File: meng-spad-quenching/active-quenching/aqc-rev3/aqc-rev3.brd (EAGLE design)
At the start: 120 x 74.9 mm, 274 parts, among them IC1 TPS7A4901, IC10 TPS7A3001, IC11 LT1534-1, IC12 74AHC1G04DCK, IC13 TLV271DBV, IC14 NC7WZ16P6X, IC15 LTC1711, IC16 HFA3134, IC17 HFA3135, IC18 USBLC6-2SC6Y, IC19 HFA3135, IC2 TPS7A4901, IC20 HFA3134, IC21 STM32F411RE, IC22 MAX572X, IC23 HFA3134, IC24 LM1117, IC25 HFA3134, IC26 THAT320, IC27 74AHC1G14DCK, IC28 NL17SZ125, IC29 TLV272DGK, IC3 LT1534-1, IC30 74AHC1G32DCK, IC31 74AHC1G08DCK, IC4 TLV272DGK, IC5 ADCMP582, IC6 DS1100LU-20+, IC7 HFA3134, IC8 NC7SV74K8X, IC9 HFA3134, M2 BSS806N, M3 BSS806N, Q6 IRLML6402TRPBF, SW1 MCU_RST, T1 MMBTH10, U1 MCP4725, U2 SN65EPT22DGK, U3 SN65EPT21DGK, X1 CONN_PULLDN_SENSE, X2 CONN_FORCE_QUENCH, X3 KEYSTONE-7774, X4 CONN_SPAD, X5 CONN_PHOTON_COUNTER, X6 KEYSTONE-7774, X7 CONN_SMU, X8 PN61729-S

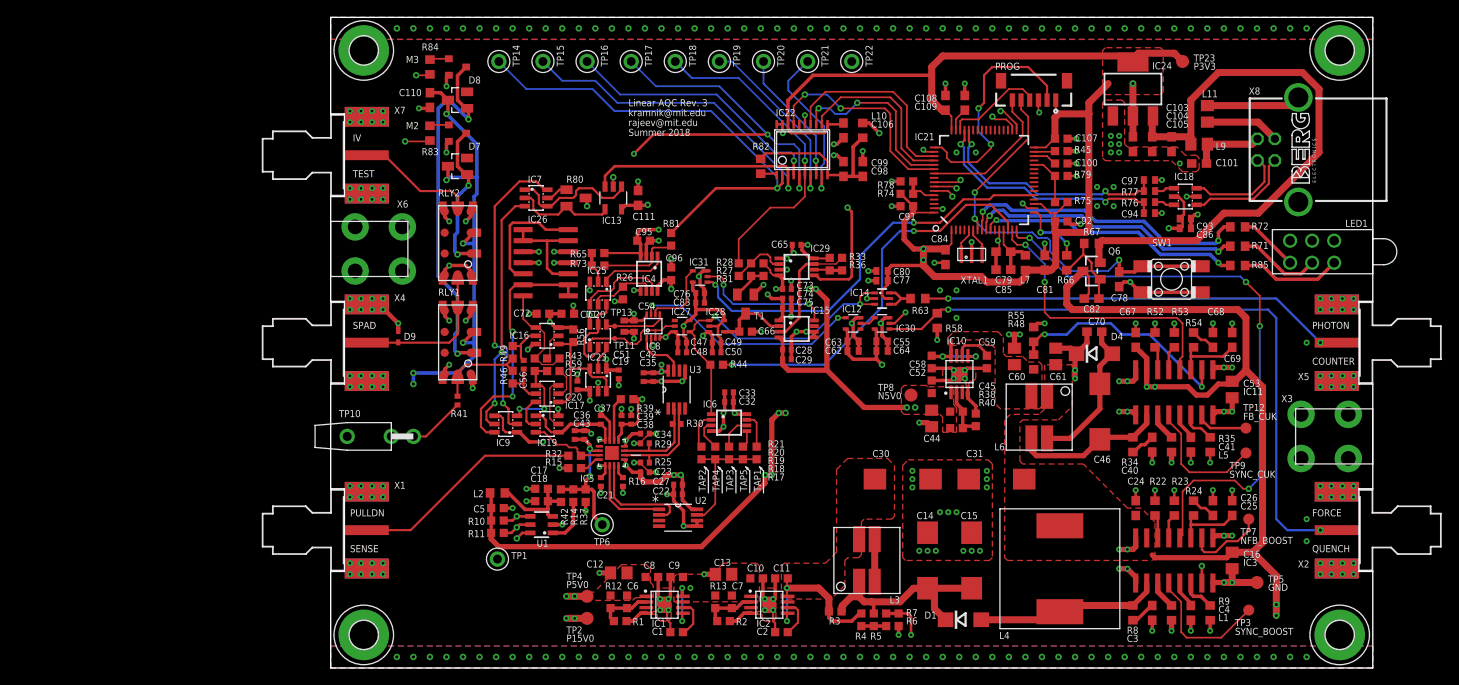
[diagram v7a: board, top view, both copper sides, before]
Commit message: Fixed one-shot error, layout done
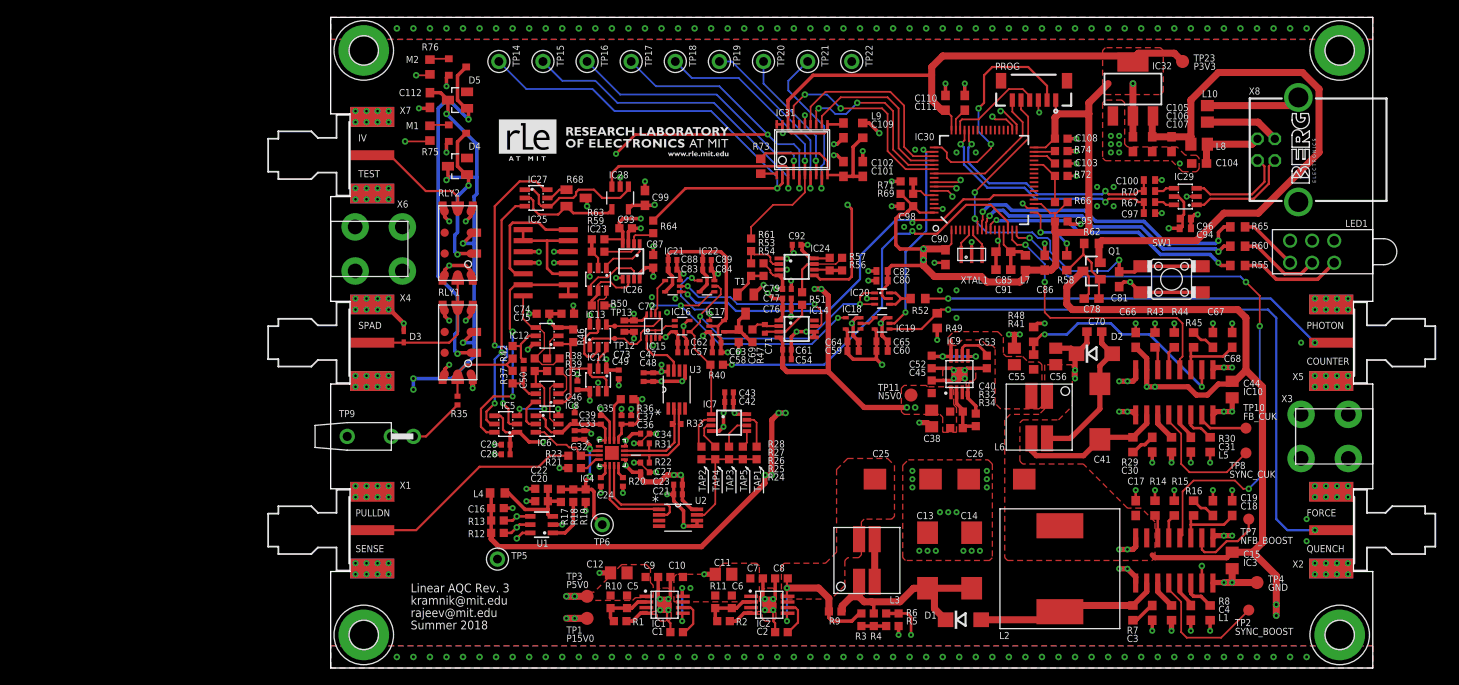
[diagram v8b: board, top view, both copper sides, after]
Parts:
- removed D7: BAS40, diode:SOT23
- removed D9: (no value), diode:SOD523
- removed L11: MI0805J102R-10, meng:R0805
- removed M3: BSS806N, meng:SOT23R_INFINEON
- removed R78: 0R, rcl-modified-footprints:R0603
- removed R79: DNP, rcl-modified-footprints:R0603
- removed R81: 220k, rcl-modified-footprints:R0603
- removed R82: 0R, rcl:R0603
- removed R83, R84: 100R, rcl:R0603
- removed R85: 470R, resistor:R0603
- added C102: 4u7, rcl:C0603
- added C112, C90: 100n, rcl:C0603
- added C87: 100n, rcl-modified-footprints:C0603
- added C88, C89: 100n, rcl-modified-footprints:C0402
- added D2: CDBA140SL-HF, diode:DO214AC
- added D3: TVS, diode:SOD523
- added DNP1000: RLE_LOGO, meng:RLE_LOGO
- added IC32: LM1117, meng:SOT-223
- added L8: MI0805J102R-10, meng:R0805
- added M1: BSS806N, meng:SOT23R_INFINEON
- added R47, R51: 0R, rcl-modified-footprints:R0603
- added R50: 110R, 1%, rcl-modified-footprints:R0603
- added R57: 100k, rcl-modified-footprints:R0603
- added R60: 470R, resistor:R0603
- added R61: 220k, rcl-modified-footprints:R0603
- added R62: 100k, resistor:R0603
- added R64: 102k, 1%, rcl-modified-footprints:R0603
- added R69: DNP, rcl-modified-footprints:R0603
- C100: value 100n -> 47p; device rcl-modified-footprints:C0603 -> rcl:C0402
- C101, C23, C28, C36, C42, C45, C7, C76, C78: value 10n -> 100n
- C103, C108, C40, C98: device rcl:C0603 -> rcl-modified-footprints:C0603
- C104, C21, C27, C29, C43, C5, C80, C83: value 100n -> 10n
- C105, C99: value 4u7 -> 100n
- C107: value 100n -> 4u7; device rcl-modified-footprints:C0603 -> rcl:C0603
- C11: value 100n -> 10u; device rcl-modified-footprints:C0603 -> rcl:C0805
- C13: value 10u -> 47u, 20V; device rcl:C0805 -> rcl:CT7343
- C15: value 47u, 20V -> 4u7; device rcl:CT7343 -> rcl:C0805
- C16: value 4u7 -> 100n; device rcl:C0805 -> rcl-modified-footprints:C0603
- C17: value 4u7 -> 100n; device rcl-modified-footprints:C0603 -> rcl:C0603
- C18: value 100n -> 15n; device rcl-modified-footprints:C0603 -> rcl:C0603
- C19: value 10n -> 220p; device rcl-modified-footprints:C0402 -> rcl:C0603
- C20: value 10n -> 100n; device rcl-modified-footprints:C0402 -> rcl-modified-footprints:C0603
- C22: value 10n -> 4u7; device rcl-modified-footprints:C0402 -> rcl-modified-footprints:C0603
- C24, C84: value 100n -> 10n; device rcl:C0603 -> rcl-modified-footprints:C0402
- C25: value 15n -> 47u, 20V; device rcl:C0603 -> rcl:CT7343
- C26: value 220p -> 47u, 20V; device rcl:C0603 -> rcl:CT7343
- C30: value 47u, 20V -> 10n; device rcl:CT7343 -> rcl:C0603
- C31: value 47u, 20V -> 1300p; device rcl:CT7343 -> rcl:C0603
- C38: value 100n -> 10u; device rcl-modified-footprints:C0402 -> rcl:C0805
- C41: value 1300p -> 68u, 16V; device rcl:C0603 -> rcl:CT7343
- C44: value 10u -> 4u7
- C46: value 68u, 16V -> 10n; device rcl:CT7343 -> rcl-modified-footprints:C0402
- C50: value 100n -> 100p
- C51: device rcl:C0402 -> rcl-modified-footprints:C0603
- C53: value 4u7 -> 10n; device rcl:C0805 -> rcl-modified-footprints:C0603
- C54, C62, C77: device rcl:C0402 -> rcl-modified-footprints:C0402
- C55: value 10n -> 10u, 10V; device rcl:C0402 -> rcl:C0805
- C56: value 100p -> 4u7; device rcl-modified-footprints:C0402 -> rcl:C0805
- C57: value 10n -> 100n; device rcl-modified-footprints:C0603 -> rcl-modified-footprints:C0402
- C58, C92: device rcl-modified-footprints:C0603 -> rcl-modified-footprints:C0402
- C59: device rcl-modified-footprints:C0603 -> rcl:C0402
- C60: value 10u, 10V -> 100n; device rcl:C0805 -> rcl:C0402
- C61: value 4u7 -> 10n; device rcl:C0805 -> rcl-modified-footprints:C0402
- C63: value 100n -> 10n; device rcl:C0402 -> rcl-modified-footprints:C0402
- C65, C73: value 100n -> 10n; device rcl-modified-footprints:C0402 -> rcl:C0402
- C66: value 100p -> 100n; device rcl-modified-footprints:C0603 -> rcl:C0603
- C67: value 100n -> 33n
- C68: value 33n -> DNP
- C69: value DNP -> 100p; device rcl:C0603 -> rcl-modified-footprints:C0603
- C71: value 100n -> DNP; device rcl-modified-footprints:C0603 -> rcl-modified-footprints:C0402
- C72: value 10n -> 100n; device rcl-modified-footprints:C0603 -> rcl:C0402
- C74, C75: device rcl-modified-footprints:C0402 -> rcl-modified-footprints:C0603
- C79: value 4u7 -> 100n; device rcl:C0603 -> rcl-modified-footprints:C0402
- C81: value 4u7 -> 10n
- C82: device rcl:C0603 -> rcl:C0402
- C85: value 100n -> 4u7
- C86: value 100n -> 4u7; device rcl:C0402 -> rcl:C0603
- C91: device rcl-modified-footprints:C0603 -> rcl:C0603
- C93: value 10n -> 100n; device rcl:C0402 -> rcl-modified-footprints:C0603
- C94: value 47p -> 100n
- C96: value 100n -> 10n; device rcl-modified-footprints:C0603 -> rcl:C0402
- D4: value CDBA140SL-HF -> BAS40; device diode:DO214AC -> diode:SOT23
- IC10: value TPS7A3001 -> LT1534-1; device Kramnik's Library:MSOP-8_POWER_PAD -> meng:SO16
- IC11: value LT1534-1 -> HFA3134; device meng:SO16 -> meng:SOT23-6L
- IC12: value 74AHC1G04DCK -> HFA3134; device 74xx-little-de:SC70-5 -> meng:SOT23-6L
- IC13: value TLV271DBV -> HFA3134; device meng:SOT23-5 -> meng:SOT23-6L
- IC14: value NC7WZ16P6X -> LTC1711; device meng:SC70-6L -> meng:MSOP8
- IC15: value LTC1711 -> NC7SV74K8X; device meng:MSOP8 -> meng:US8_3.1MM_JDEC_MO-187
- IC16: value HFA3134 -> 74AHC1G14DCK; device meng:SOT23-6L -> 74xx-little-de:SC70-5
- IC17: value HFA3135 -> NL17SZ125; device meng:SOT23-6L -> 74xx-little-de:SC70-5
- IC18: value USBLC6-2SC6Y -> 74AHC1G04DCK; device meng:SOT23-6L -> 74xx-little-de:SC70-5
- IC19: value HFA3135 -> 74AHC1G32DCK; device meng:SOT23-6L -> 74xx-little-de:SC70-5
- IC20: value HFA3134 -> NC7WZ16P6X; device meng:SOT23-6L -> meng:SC70-6L
- IC21: value STM32F411RE -> 74AHC1G08DCK; device meng:TQFP64_STM32 -> 74xx-little-de:SC70-5
- IC22: value MAX572X -> 74AHC1G08DCK; device meng:TSSOP20 -> 74xx-little-de:SC70-5
- IC24: value LM1117 -> TLV272DGK; device meng:SOT-223 -> meng:MSOP8
- IC25: value HFA3134 -> THAT320; device meng:SOT23-6L -> meng:SO14
- IC26: value THAT320 -> TLV272DGK; device meng:SO14 -> meng:MSOP8
- IC27: value 74AHC1G14DCK -> HFA3134; device 74xx-little-de:SC70-5 -> meng:SOT23-6L
- IC28: value NL17SZ125 -> TLV271DBV; device 74xx-little-de:SC70-5 -> meng:SOT23-5
- IC29: value TLV272DGK -> USBLC6-2SC6Y; device meng:MSOP8 -> meng:SOT23-6L
- IC30: value 74AHC1G32DCK -> STM32F411RE; device 74xx-little-de:SC70-5 -> meng:TQFP64_STM32
- IC31: value 74AHC1G08DCK -> MAX572X; device 74xx-little-de:SC70-5 -> meng:TSSOP20
- IC4: value TLV272DGK -> ADCMP582; device meng:MSOP8 -> meng:QFN50P300X300X80-16N
- IC5: value ADCMP582 -> HFA3134; device meng:QFN50P300X300X80-16N -> meng:SOT23-6L
- IC6: value DS1100LU-20+ -> HFA3135; device meng:MSOP8 -> meng:SOT23-6L
- IC7: value HFA3134 -> DS1100LU-20+; device meng:SOT23-6L -> meng:MSOP8
- IC8: value NC7SV74K8X -> HFA3135; device meng:US8_3.1MM_JDEC_MO-187 -> meng:SOT23-6L
- IC9: value HFA3134 -> TPS7A3001; device meng:SOT23-6L -> Kramnik's Library:MSOP-8_POWER_PAD
- L10: value PE-0603FB601ST -> MI0805J102R-10; device meng:R0603 -> meng:R0805
- L2: value PE-0603FB601ST -> 732-1699-2-ND; device meng:R0603 -> meng:WE_INDUCTOR_SIZE_CODE_1210
- L4: value 732-1699-2-ND -> PE-0603FB601ST; device meng:WE_INDUCTOR_SIZE_CODE_1210 -> meng:R0603
- L9: value MI0805J102R-10 -> PE-0603FB601ST; device meng:R0805 -> meng:R0603
- R10: value 2k2 -> 76k8
- R11: value 2k2 -> 137k
- R12: value 76k8 -> 2k2
- R13: value 137k -> 2k2
- R14: device rcl-modified-footprints:R0603 -> resistor:R0603
- R15: value DNP -> 1k; device rcl-modified-footprints:R0603 -> resistor:R0603
- R16: value 49R9 -> 6k8; device rcl-modified-footprints:R0402 -> resistor:R0603
- R18: value DNP -> 1k
- R20: value DNP -> 49R9; device rcl-modified-footprints:R0603 -> rcl-modified-footprints:R0402
- R22: value 1k -> 150R; device resistor:R0603 -> rcl-modified-footprints:R0402
- R23: value 1k -> 220R, 1%; device resistor:R0603 -> rcl-modified-footprints:R0603
- R24: value 6k8 -> DNP; device resistor:R0603 -> rcl-modified-footprints:R0603
- R25: value 150R -> DNP; device rcl-modified-footprints:R0402 -> rcl-modified-footprints:R0603
- R26: value 220R -> DNP
- R27, R28: value 220k -> DNP
- R29: value 150R -> 100R; device rcl-modified-footprints:R0402 -> resistor:R0603
- R3, R74: value DNP -> 0R
- R30: value 100R -> 16k9; device rcl-modified-footprints:R0402 -> rcl:R0603
- R31: value 10k -> 150R; device rcl-modified-footprints:R0603 -> rcl-modified-footprints:R0402
- R32: value 220R -> 76k8
- R33: value 100k -> 100R; device rcl-modified-footprints:R0603 -> rcl-modified-footprints:R0402
- R34: value 100R -> 24k; device resistor:R0603 -> rcl-modified-footprints:R0603
- R35: value 16k9 -> 49R9; device rcl:R0603 -> rcl-modified-footprints:R0402
- R36: value 100k -> 10k
- R37, R42: value DNP -> 100R, 1%
- R38: value 76k8 -> 200R, 1%
- R39: value 10k -> 200R, 1%
- R4: value 0R -> DNP
- R40: value 24k -> 49R9
- R41: value 49R9 -> 1k4; device rcl-modified-footprints:R0402 -> resistor:R0603
- R43: value 220R -> 1k; device rcl-modified-footprints:R0603 -> resistor:R0603
- R44: value 49R9 -> 1k; device rcl-modified-footprints:R0603 -> resistor:R0603
- R45: value 0R -> 2k; device rcl-modified-footprints:R0603 -> rcl:R0603
- R46: value 100R -> 220R, 1%
- R48: value 1k4 -> 1k
- R49: value 100R -> 49R9; device rcl-modified-footprints:R0603 -> rcl:R0603
- R5: value DNP -> 29k4
- R52: value 1k -> 49R9; device resistor:R0603 -> rcl:R0603
- R53: value 1k -> 220k; device resistor:R0603 -> rcl-modified-footprints:R0603
- R54: value 2k -> 10k; device rcl:R0603 -> rcl-modified-footprints:R0603
- R55: value 1k -> 470R
- R56: value 220R -> 100k
- R58: value 49R9 -> 4k7; device rcl:R0603 -> resistor:R0603
- R59: value 220R -> 127k, 1%
- R6: value 29k4 -> 2k49
- R63: value 49R9 -> 274R, 1%; device rcl:R0603 -> rcl-modified-footprints:R0603
- R65: value 220R -> 470R; device rcl-modified-footprints:R0603 -> resistor:R0603
- R66: value 4k7 -> DNP; device resistor:R0603 -> rcl-modified-footprints:R0603
- R67: value 100k -> 22R; device resistor:R0603 -> resistor:R0402
- R7: value 2k49 -> 10R; device rcl-modified-footprints:R0603 -> resistor:R0603
- R71: value 470R -> 0R; device resistor:R0603 -> rcl-modified-footprints:R0603
- R72: value 470R -> DNP; device resistor:R0603 -> rcl-modified-footprints:R0603
- R73: value 220k -> 0R; device rcl-modified-footprints:R0603 -> rcl:R0603
- R75: value DNP -> 100R; device rcl-modified-footprints:R0603 -> rcl:R0603
- R76: value 22R -> 100R; device resistor:R0402 -> rcl:R0603
- R8: value 10R -> 16k9
- R9: value 16k9 -> DNP; device resistor:R0603 -> rcl-modified-footprints:R0603
- TP1: value GND -> TPTP15R; device Kramnik's Library:KEYSTONE_5000_MINIATURE -> testpad:TP15R
- TP10: value TP_VSCOPE -> TPB1,27; device meng:JOHNSON-129-0701-30X -> testpad:B1,27
- TP11: value TPTP06R -> TPTP15R; device testpad:TP06R -> testpad:TP15R
- TP12: value TPB1,27 -> TPTP06R; device testpad:B1,27 -> testpad:TP06R
- TP2, TP8: value TPTP15R -> TPB1,27; device testpad:TP15R -> testpad:B1,27
- TP3: value TPB1,27 -> TPTP15R; device testpad:B1,27 -> testpad:TP15R
- TP5: value TPTP15R -> GND; device testpad:TP15R -> Kramnik's Library:KEYSTONE_5000_MINIATURE
- TP9: value TPB1,27 -> TP_VSCOPE; device testpad:B1,27 -> meng:JOHNSON-129-0701-30X
- moved TP9 95.9 mm to (9.53, 26.7), turned to 180 degrees
- moved TP10 95.9 mm to (105.4, 27.6), turned to 0 degrees
- moved TP5 87.5 mm to (19.2, 12.5), turned to 270 degrees
- moved R35 86.8 mm to (14.6, 30.8), turned to 270 degrees
- moved C16 84.8 mm to (19.2, 18.4), turned to 0 degrees
- moved R76 84.3 mm to (11.4, 69.2), turned to 270 degrees
- moved C18 77.3 mm to (101.6, 18.4), turned to 90 degrees
- moved TP4 77.2 mm to (106.7, 9.84)
- moved D4 76.5 mm to (14.6, 57.8), turned to 90 degrees
- moved TP3 76.2 mm to (29.5, 8.26)
- moved TP2 76.2 mm to (105.7, 6.67)
- moved R65 73.7 mm to (104.5, 50.8)
- moved TP12 73.4 mm to (32.7, 37.9)
- moved R75 73.1 mm to (11.4, 61.6), turned to 270 degrees
- moved C19 72.3 mm to (103.8, 18.4), turned to 90 degrees
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- renumbered D8 to D5, Q6 to Q1, R77 to R70, R80 to R68
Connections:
- new net CAP_!RESET: IC17.1, IC22.4
- new net N$11: C71.2, IC14.3, R51.1
- new net N$13: C71.1, IC14.2, R47.1
- net !FORCE_QUENCH: now also IC15.7, IC18.4, IC22.1; no longer IC12.4, IC8.7
- net !LOGIC_QUENCH: now also IC13.1, IC15.3, IC16.2, TP12.TP; no longer IC20.1, IC27.2, IC8.3, TP11.TP
- net !MCU_SHDN_BOOST: now also IC30.16; no longer IC21.16
- net !MCU_SHDN_CUK: now also IC10.12, IC30.15; no longer IC11.12, IC21.15
- net !MCU_SMPS_PRECHG: now also IC30.17, R58.2; no longer IC21.17, R66.2
- net !ONE_SHOT_CLR: now also IC14.7, IC21.2; no longer IC15.8, IC31.2
- net BLANKING_LATCH_EN: now also R24.1, R25.1, R26.1, R27.1, R28.1; no longer R17.1, R18.1, R19.1, R20.1, R21.1
- net BOOST_STAGE1: now also C13.+, R4.1, R9.1; no longer C15.+, R3.1, R5.1
- net BOOST_SW_NODE: now also L2.2, R7.1; no longer L4.2, R8.1
- net CCS_STEERING_TAIL: now also IC13.2, IC13.5, IC23.6; no longer IC20.2, IC20.5, IC25.6
- net CCS_VA_SETPOINT: now also IC11.5, IC23.3; no longer IC23.5, IC25.3
- net COMP_HYS: now also IC4.14, R36.2; no longer IC5.14, R39.2
- net COMP_LE_N: now also IC4.6; no longer IC5.6
- net COMP_LE_P: now also IC4.7; no longer IC5.7
- net COMP_Q_N: now also IC4.10, R22.1, R33.1; no longer IC5.10, R25.1, R30.1
- net COMP_Q_P: now also IC4.11, R31.1, R33.2; no longer IC5.11, R29.1, R30.2
- net COMP_VTN: now also IC4.4, R21.2; no longer IC5.4, R15.2
- net COMP_VTT: now also IC4.8, R20.1; no longer IC5.8, R16.1
- net DAC1_!CLR: now also IC30.54, IC31.17; no longer IC21.54, IC22.17
- net DAC1_DIN: now also IC30.53, IC31.13; no longer IC21.53, IC22.13
- net DAC1_DOUT: now also IC30.52, IC31.12; no longer IC21.52, IC22.12
- net DAC1_SCLK: now also IC30.51, IC31.14; no longer IC21.51, IC22.14
- net DAC2_ADDRSEL: now also IC30.57; no longer IC21.57
- net DAC2_SCL: now also IC30.58, R12.2; no longer IC21.58, R11.2
- net DAC2_SDA: now also IC30.59, R13.2; no longer IC21.59, R10.2
- net DELTAV_BASE: now also IC23.1, IC26.1; no longer IC25.1, IC4.1
- net DELTAV_FB: now also IC23.2, R59.1, R63.2; no longer IC25.2, R65.2, R73.1
- net DELTAV_VGND: now also IC26.2, R59.2, R64.1; no longer IC4.2, R73.2, R81.1
- net DFLOP_!CLR: now also IC15.6, IC21.4; no longer IC31.4, IC8.6
- net DIAMOND_BASE: now also IC27.1, IC27.4, IC28.1; no longer IC13.1, IC7.1, IC7.4
- net DIAMOND_FB: now also IC27.2, IC28.4; no longer IC13.4, IC7.2
- net DIAMOND_FB_R: now also IC27.5; no longer IC7.5
- net DIAMOND_IBIAS_BOTTOM: now also C51.2, IC5.3, IC8.4, R38.1; no longer C57.2, IC17.4, IC9.3, R43.1
- net DIAMOND_IBIAS_MID: now also IC25.6, IC25.8, IC25.9, IC5.6; no longer IC26.6, IC26.8, IC26.9, IC9.6
- net DIAMOND_IBIAS_TOP: now also C51.1, IC12.4, IC25.7, R39.2; no longer C57.1, IC16.4, IC26.7, R59.2
- net DIAMOND_IN: now also IC11.3, IC11.6, IC12.1, IC8.1, R46.1; no longer IC16.1, IC17.1, IC23.3, IC23.6, R56.1
- net DMD_IN_CASC: now also IC6.2, IC8.6; no longer IC17.6, IC19.2
- net DMD_IN_NPN_E: now also IC12.2, R38.2; no longer IC16.2, R43.2
- net DMD_IN_PNP_E: now also IC8.2, R39.1; no longer IC17.2, R59.1
- net DMD_OP_CASC: now also IC6.5, IC8.3; no longer IC17.3, IC19.5
- net DMD_OP_NPN: now also C50.1, IC12.5, R42.2; no longer C56.1, IC16.5, R49.2
- net DMD_OP_PNP: now also C50.2, IC8.5, R37.1; no longer C56.2, IC17.5, R46.1
- net DMD_OUT: now also R35.1, R37.2, R42.1; no longer R41.1, R46.2, R49.1
- net FORCE_QUENCH: now also IC18.2, IC19.4; no longer IC12.2, IC30.4
- net FORCE_QUENCH_USER: now also IC19.1, R49.2; no longer IC30.1, R58.2
- net GND: now also C102.2, C112.2, C13.-, C15.2, C25.-, C26.-, C30.2, C31.2, C45.2, C46.2, C56.2, C57.2, C7.2, C82.2, C87.2, C88.2, C89.2, C90.2, D2.C, D3.A, IC10.1, IC10.16, IC10.8, IC10.9, IC14.5, IC14.6, IC15.4, IC16.3, IC17.3, IC18.3, IC19.3, IC20.2, IC21.3, IC22.3, IC24.3, IC25.11, IC25.4, IC26.3, IC28.2, IC29.2, IC30.12, IC30.18, IC30.63, IC31.15, IC31.19, IC31.20, IC32.1, IC4.15, IC6.6, IC7.4, IC9.4, IC9.PAD, L10.2, M1.2, R14.2, R15.2, R19.1, R20.2, R21.1, R30.1, R31.2, R34.2, R43.2, R44.2, R48.2, R49.1, R50.1, R6.2, R71.2, R72.2, R74.2, R8.1, TP4.TP, TP5.P$1, TP9.GND1, TP9.GND2; no longer C13.2, C15.-, C25.2, C26.2, C30.-, C31.-, C40.2, C41.2, C5.2, C50.2, C51.2, C71.2, C78.2, D4.C, D9.A, IC10.4, IC10.PAD, IC11.1, IC11.16, IC11.8, IC11.9, IC12.3, IC13.2, IC14.2, IC15.5, IC15.6, IC18.2, IC19.6, IC21.12, IC21.18, IC21.63, IC22.15, IC22.19, IC22.20, IC24.1, IC26.11, IC26.4, IC27.3, IC28.3, IC29.3, IC30.3, IC31.3, IC4.3, IC5.15, IC6.4, IC8.4, L11.2, M3.2, R15.1, R16.2, R23.2, R25.2, R26.1, R29.2, R35.1, R37.1, R40.2, R45.2, R52.2, R53.2, R55.2, R58.1, R7.2, R78.2, R79.2, R9.1, TP1.P$1, TP10.GND1, TP10.GND2, TP5.TP
- net HOLDOFF_TRIG: now also IC15.1; no longer IC8.1
- net LDO_N10V0_FB_CH1: now also C40.2, IC9.2, R32.1, R34.1; no longer C45.2, IC10.2, R38.1, R40.1
- net LDO_N10V0_NR_SS_CH1: now also C53.1, IC9.6; no longer C59.1, IC10.6
- net LDO_P10V0_FB_CH1: now also C6.2, R11.1; no longer C7.2, R13.1
- net LDO_P5V0_FB_CH1: now also C5.2, R10.1; no longer C6.2, R12.1
- net LOGIC_QUENCH: now also IC13.4, IC15.5; no longer IC20.4, IC8.5
- net LOGIC_QUENCH_BUF: now also IC16.4, IC20.1, IC20.3, IC22.2, IC7.1, R40.2; no longer IC14.1, IC14.3, IC27.4, IC28.1, IC6.1, R44.2
- net MCU_AQC_RLY: now also IC30.34, R76.2; no longer IC21.34, R84.2
- net MCU_BOOT0: now also IC30.60, R69.2, R71.1; no longer IC21.60, R74.2, R78.1
- net MCU_BOOT1: now also IC30.28, R66.2, R72.1; no longer IC21.28, R75.2, R79.1
- net MCU_IVTEST_RLY: now also IC30.33, R75.2; no longer IC21.33, R83.2
- net MCU_JTCK: now also IC30.49; no longer IC21.49
- net MCU_JTDO: now also IC30.55; no longer IC21.55
- net MCU_JTMS: now also IC30.46; no longer IC21.46
- net MCU_LED1: now also IC30.8, R65.2; no longer IC21.8, R72.2
- net MCU_LED2: now also IC30.9, R60.2; no longer IC21.9, R71.2
- net MCU_LED3: now also IC30.10, R55.2; no longer IC21.10, R85.2
- net MCU_NRST: now also C81.1, IC30.7; no longer C78.1, IC21.7
- net MCU_OSC_IN: now also IC30.5; no longer IC21.5
- net MCU_OSC_OUT: now also IC30.6; no longer IC21.6
- net MCU_PB11: now also C103.1, IC30.30; no longer C100.1, IC21.30
- net MCU_TIM2_CH1_IN: now also IC30.14, R40.1; no longer IC21.14, R44.1
- net MCU_TIM2_CH1_OUT_1: now also IC21.1, IC30.21; no longer IC21.21, IC31.1
- net MCU_TIM2_CH1_OUT_2: now also IC19.2, IC30.50; no longer IC21.50, IC30.2
- net MCU_USB_FS_D_N: now also C100.1, IC30.44; no longer C97.1, IC21.44
- net MCU_USB_FS_D_P: now also C97.1, IC30.45, R67.1; no longer C94.1, IC21.45, R76.1
- net MCU_VCAP_1: now also IC30.31, R74.1; no longer IC21.31, R45.1
- net MCU_VCAP_2: now also C111.1, IC30.47; no longer C109.1, IC21.47
- net N$1: now also R18.2; no longer R14.2
- net N$10: now also IC24.6, R56.1, R57.2; no longer IC29.6, R33.2, R36.1
- net N$12: now also C78.1, R58.1, R62.1; no longer C82.1, R66.1, R67.1
- net N$15: now also M1.1, R75.1; no longer M2.1, R83.1
- net N$16: now also IC27.6, IC5.2; no longer IC7.6, IC9.2
- net N$18: now also R5.1; no longer R7.1
- net N$20: now also IC10.3; no longer IC11.3
- net N$24: now also R60.1; no longer R71.1
- net N$26: now also IC27.3, IC5.5; no longer IC7.3, IC9.5
- net N$29: now also IC20.4, IC20.6, R52.2; no longer IC14.4, IC14.6, R63.2
- net N$3: now also M2.1, R76.1; no longer M3.1, R84.1
- net N$31: now also R55.1; no longer R85.1
- net N$4: now also M2.3; no longer M3.3
- net N$5: now also IC24.1; no longer IC29.1
- net N$51: now also R15.1; no longer R23.1
- net N$52: now also R14.1; no longer R22.1
- net N$54: now also R7.2; no longer R8.2
- net N$55: now also C18.1, R16.1; no longer C25.1, R24.1
- net N$56: now also C19.1, R16.2; no longer C26.1, R24.2
- net N$57: now also R8.2; no longer R9.2
- net N$6: now also D4.1, M1.3; no longer D7.1, M2.3
- net N$60: now also IC10.13, R44.1; no longer IC11.13, R53.1
- net N$61: now also IC10.14, R43.1; no longer IC11.14, R52.1
- net N$62: now also C30.1, R29.2; no longer C40.1, R34.2
- net N$63: now also C67.1, R45.1; no longer C68.1, R54.1
- net N$64: now also C68.1, IC10.11, R45.2; no longer C69.1, IC11.11, R54.2
- net N$65: now also IC10.6, R30.2; no longer IC11.6, R35.2
- net N$67: now also IC10.10, R41.2, R48.1; no longer IC11.10, R48.2, R55.1
- net N$68: now also C41.+, IC10.2, R29.1; no longer C46.+, IC11.2, R34.1
- net N$69: now also C41.-, D2.A; no longer C46.-, D4.A
- net N$7: now also IC24.7, R51.2, R57.1; no longer IC15.3, IC29.7, R33.1
- net N$73: now also R3.2; no longer R6.2
- net N$8: now also C31.1, IC10.5; no longer C41.1, IC11.5
- net N$88: now also IC25.1, IC25.10, IC25.13, IC25.2; no longer IC26.1, IC26.10, IC26.13, IC26.2
- net N$89: now also IC25.14, IC25.5; no longer IC26.14, IC26.5
- net N$9: now also R65.1; no longer R72.1
- net N$92: now also IC31.1, R73.2; no longer IC22.1, R82.2
- net NC_DAC1_IRQ: now also IC31.16; no longer IC22.16
- net NC_ONE_SHOT_CLR: now also IC14.8; no longer IC15.7
- net ONE_SHOT_CAP: now also C69.1, IC17.4, R47.2; no longer C66.1, IC15.2, IC28.4
- net ONE_SHOT_FB: now also R53.1, R54.1; no longer R27.1, R31.1
- net ONE_SHOT_VGND: now also IC24.2, R53.2, R61.1; no longer IC29.2, R27.2, R28.1
- net PHOTON_COUNT_OUT: now also R52.1; no longer R63.1
- net PP_N5V0_ANALOG: now also C36.1, C37.1, C40.1, C54.1, C61.1, C79.1, C93.1, IC14.4, IC24.4, IC26.4, IC4.13, IC9.1, R32.2, R36.1, R54.2, R63.1, TP11.TP; no longer C28.1, C29.1, C39.1, C44.1, C52.1, C73.1, C95.1, IC10.1, IC15.4, IC29.4, IC4.4, IC5.13, R31.2, R38.2, R39.1, R65.1, TP8.TP
- net PP_N6V0_CUK: now also C52.1, C55.1, IC9.5, IC9.8, R41.1; no longer C58.1, C60.1, IC10.5, IC10.8, R48.1
- net PP_P15V0_ANALOG: now also C11.1, C6.1, C74.1, C75.1, IC12.3, IC12.6, IC25.12, IC25.3, R11.2, R46.2, TP1.TP; no longer C13.1, C71.1, C72.1, C9.1, IC16.3, IC16.6, IC26.12, IC26.3, R13.2, R56.2, TP2.TP
- net PP_P16V0_BOOST: now also C25.+, C8.1, R3.1, R9.2; no longer C11.1, C30.+, R3.2, R4.1
- net PP_P3V3: now also C105.1, C109.1, C110.1, C16.1, C21.1, C43.1, C57.1, C58.1, C59.1, C60.1, C65.1, C72.1, C73.1, C82.1, C88.1, C89.1, C90.1, C94.1, C95.1, C96.1, C98.1, IC15.2, IC15.8, IC16.5, IC17.2, IC17.5, IC19.5, IC20.5, IC21.5, IC22.5, IC29.5, IC30.1, IC30.19, IC30.32, IC30.48, IC30.64, IC31.11, IC31.18, IC32.2, IC32.4, IC4.12, IC4.9, IC7.8, L4.1, R12.1, R13.1, R66.1, R69.1; no longer C103.1, C106.1, C107.1, C22.1, C32.1, C33.1, C35.1, C49.1, C5.1, C50.1, C51.1, C54.1, C55.1, C76.1, C77.1, C81.1, C91.1, C92.1, C93.1, IC12.5, IC14.5, IC21.1, IC21.19, IC21.32, IC21.48, IC21.64, IC22.11, IC22.18, IC24.2, IC24.4, IC27.5, IC28.2, IC28.5, IC30.5, IC31.5, IC5.12, IC5.9, IC6.8, IC8.2, IC8.8, L2.1, R10.1, R11.1, R74.1, R75.1
- net PP_P3V3_AV_DET_DAC: now also C20.1, C22.1, L4.2, R17.2; no longer C17.1, C18.1, L2.2, R42.2
- net PP_P3V3_VDDA: now also C91.1, IC30.13; no longer C79.1, IC21.13
- net PP_P5V0_ANALOG: now also C24.1, C28.1, C29.1, C35.1, C39.1, C46.1, C49.1, C5.1, C76.1, C77.1, C87.1, C9.1, C92.1, C99.1, IC11.1, IC11.4, IC13.6, IC14.1, IC24.8, IC26.8, IC28.5, IC4.16, IC4.5, IC5.1, IC5.4, IC6.1, IC6.4, L9.1, R10.2, R56.2, TP3.TP; no longer C111.1, C19.1, C20.1, C21.1, C37.1, C6.1, C65.1, C74.1, C75.1, C8.1, C96.1, IC13.5, IC15.1, IC19.1, IC19.4, IC20.6, IC23.1, IC23.4, IC29.8, IC4.8, IC5.16, IC5.5, IC9.1, IC9.4, L10.1, R12.2, R36.2, TP4.TP
- net PP_P5V0_DAC1: now also C101.1, C102.1, IC31.10, L9.2, R73.1; no longer C98.1, C99.1, IC22.10, L10.2, R82.1
- net PULLDN_SENSE_R_CONN: now also R23.1; no longer R32.1
- net SMPS_USB_VDD: now also C112.1, C15.1, C17.1, C26.+, C44.1, C56.1, C66.1, C78.2, D4.3, IC10.15, L2.1; no longer C110.1, C16.1, C24.1, C31.+, C53.1, C61.1, C67.1, C82.2, D7.3, IC11.15, L4.1
- net SPAD_PULLDN_SENSE: now also IC4.3, IC6.3, R23.2; no longer IC19.3, IC5.3, R32.2
- net STEERING_CASC: now also IC11.2, IC13.3; no longer IC20.3, IC23.2
- net TAP1: now also IC7.7, R28.2; no longer IC6.7, R21.2
- net TAP2: now also IC7.2, R24.2; no longer IC6.2, R17.2
- net TAP3: now also IC7.6, R26.2; no longer IC6.6, R19.2
- net TAP4: now also IC7.3, R25.2; no longer IC6.3, R18.2
- net TAP5: now also IC7.5, R27.2; no longer IC6.5, R20.2
- net TP_FB_CUK: now also IC10.7, TP10.TP; no longer IC11.7, TP12.TP
- net TP_SYNC_BOOST: now also TP2.TP; no longer TP3.TP
- net TP_SYNC_CUK: now also IC10.4, TP8.TP; no longer IC11.4, TP9.TP
- net USBCONN_P1: now also C104.1, L8.1; no longer C101.1, L9.1
- net USBCONN_P4: now also L10.1; no longer L11.1
- net USBD_CONN_N: now also IC29.3; no longer IC18.3
- net USBD_CONN_P: now also IC29.1; no longer IC18.1
- net USBD_TVS_N: now also IC29.4; no longer IC18.4
- net USBD_TVS_P: now also IC29.6, R67.2; no longer IC18.6, R76.2
- net USB_VDD: now also C106.1, C107.1, IC32.3, L8.2, R62.2; no longer C104.1, C105.1, IC24.3, L9.2, R67.2
- net VA_BASE: now also IC23.4, IC26.7; no longer IC25.4, IC4.7
- net VA_FB: now also IC23.5, IC26.6, R50.2; no longer IC25.5, IC4.6, R26.2
- net VREF_AV_DET: now also C32.1, C33.1, IC4.2, R17.1, R18.1, R19.2; no longer C36.1, C43.1, IC5.2, R14.1, R37.2, R42.1
- net VREF_DELTAV_SETPOINT: now also IC31.2, R64.2; no longer IC22.2, R81.2
- net VREF_DIAMOND_IBIAS: now also IC28.3, IC31.3; no longer IC13.3, IC22.3
- net VREF_EXTRA_2: now also IC31.7; no longer IC22.7
- net VREF_EXTRA_3: now also IC31.8; no longer IC22.8
- net VREF_EXTRA_4: now also IC31.9; no longer IC22.9
- net VREF_ONE_SHOT_CCS: now also IC31.6, R61.2; no longer IC22.6, R28.2
- net VREF_ONE_SHOT_COMP: now also IC24.5, IC31.4; no longer IC22.4, IC29.5
- net VREF_VA_SETPOINT: now also IC26.5, IC31.5; no longer IC22.5, IC4.5
- net V_SCOPE: now also R35.2, TP9.SIG; no longer R41.2, TP10.SIG
- net V_SPAD: now also D3.C; no longer D9.C
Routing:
- net PP_P3V3: track 367.6 -> 391.1 mm, vias 19 -> 20
- net CAP_!RESET: track 0.00 -> 8.88 mm, vias 0 -> 2
- net PP_P5V0_ANALOG: track 173.1 -> 180.8 mm
- net N$11: track 0.00 -> 6.33 mm
- net N$7: track 14.0 -> 7.79 mm
- net LOGIC_QUENCH_BUF: track 38.3 -> 43.5 mm
- net !FORCE_QUENCH: track 26.5 -> 31.0 mm, vias 2 -> 3
- net DFLOP_!CLR: track 8.38 -> 4.37 mm
- net !ONE_SHOT_CLR: track 16.2 -> 19.9 mm
- net VREF_ONE_SHOT_CCS: track 37.3 -> 33.6 mm
- net GND: track 296.6 -> 300.1 mm, vias 370 -> 380
- net N$13: track 0.00 -> 3.34 mm
- net VA_BASE: track 10.3 -> 7.55 mm
- net MCU_TIM2_CH1_OUT_1: track 46.7 -> 49.1 mm
- net DELTAV_VGND: track 9.57 -> 7.35 mm
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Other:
- outline, holes or cut-outs redrawn
- board text added: "Linear Active Quenching Circuit Rev. 3 kramnik@mit.edu rajeev@mit.edu Summer 2018"
- board text removed: "Linear Active SPAD Quenching Circuit Rev. 3 kramnik@mit.edu rajeev@mit.edu Summer 2018"
